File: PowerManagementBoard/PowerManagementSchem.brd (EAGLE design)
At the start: 160 x 100 mm, 95 parts, among them J1 D15S24A4GV00LF, U1 VX7805-500, U2 PYB20-Q24-S5, U3 PYB30-Q48-S5, U4 PYB30-Q48-S12, U5 3V3REG, U6 INA4180-SPLIT, U7 INA4180-SPLIT, U8 TEENSY-4.0SILK, U9 INA4180-SPLIT

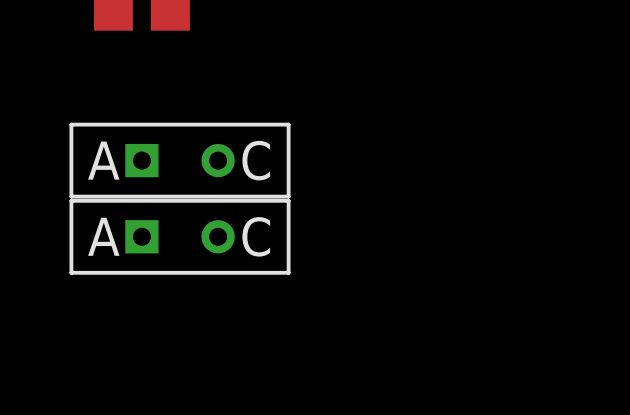
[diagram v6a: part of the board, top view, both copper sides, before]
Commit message: Added useless LED for test, names some nets.
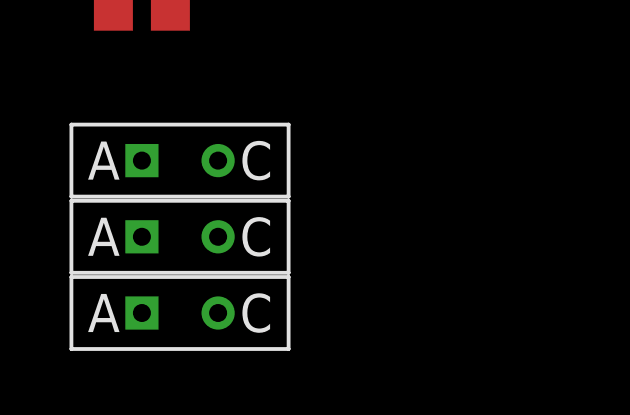
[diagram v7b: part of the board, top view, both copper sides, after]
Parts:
- added U$25: FLAT_LED, PowerManagementParts:FLAT_LED
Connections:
- removed net N$35: R20.1, U9.9
- removed net N$37: R21.1, U9.13
- removed net N$42: RN4.13, U$23.3
- net 12V: now also RN4.13, U$23.3
- net 12V-CAM: now also R20.1, U9.9
- net 12V-STA: now also R21.1, U9.13
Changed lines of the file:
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@@
 </element>
 <element name="U$21" library="PowerManagementParts" package="FLAT_LED" value="FLAT_LED" x="-261.62" y="-593.09"/>
+<element name="U$25" library="PowerManagementParts" package="FLAT_LED" value="FLAT_LED" x="-261.62" y="-595.63"/>
 </elements>
 <signals>
@@
 <contactref element="RN4" pad="14"/>
 <contactref element="U$22" pad="3"/>
+<contactref element="RN4" pad="13"/>
+<contactref element="U$23" pad="3"/>
+<wire x1="-225.425" y1="-529.7678" x2="-226.695" y2="-529.7678" width="0" layer="19" extent="1-1"/>
 <wire x1="-242.83" y1="-551.41" x2="-226.695" y2="-529.7678" width="0" layer="19" extent="1-1"/>
-<wire x1="-158.75" y1="-471.17" x2="-226.695" y2="-529.7678" width="0" layer="19" extent="1-1"/>
+<wire x1="-242.83" y1="-571.73" x2="-242.83" y2="-551.41" width="0" layer="19" extent="1-1"/>
+<wire x1="-158.75" y1="-471.17" x2="-225.425" y2="-529.7678" width="0" layer="19" extent="1-1"/>
 <wire x1="30.48" y1="74.93" x2="-158.75" y2="-471.17" width="0" layer="19" extent="1-1"/>
 <wire x1="-34.61" y1="149.86" x2="30.48" y2="74.93" width="0" layer="19" extent="1-1"/>
@@
 <signal name="12V-CAM">
 <contactref element="U$11" pad="PIN1"/>
+<contactref element="R20" pad="1"/>
+<contactref element="U9" pad="9"/>
+<wire x1="-242.722" y1="-556.26" x2="-227.33" y2="-509.0922" width="0" layer="19" extent="1-1"/>
+<wire x1="-147.828" y1="-422.91" x2="-227.33" y2="-509.0922" width="0" layer="19" extent="1-1"/>
 </signal>
 <signal name="12V-STA">
 <contactref element="U$12" pad="PIN1"/>
+<contactref element="R21" pad="1"/>
+<contactref element="U9" pad="13"/>
+<wire x1="-242.722" y1="-576.58" x2="-229.87" y2="-509.0922" width="0" layer="19" extent="1-1"/>
+<wire x1="-147.828" y1="-440.69" x2="-229.87" y2="-509.0922" width="0" layer="19" extent="1-1"/>
 </signal>
 <signal name="5V-DIG-STA">
@@
 <wire x1="-239.878" y1="-556.26" x2="-245.11" y2="-544.512" width="0" layer="19" extent="1-1"/>
 </signal>
-<signal name="N$35">
-<contactref element="R20" pad="1"/>
-<contactref element="U9" pad="9"/>
-<wire x1="-242.722" y1="-556.26" x2="-227.33" y2="-509.0922" width="0" layer="19" extent="1-1"/>
-</signal>
 <signal name="N$36">
 <contactref element="U$23" pad="4"/>
@@
 <wire x1="-239.878" y1="-576.58" x2="-245.11" y2="-564.832" width="0" layer="19" extent="1-1"/>
 </signal>
-<signal name="N$37">
-<contactref element="R21" pad="1"/>
-<contactref element="U9" pad="13"/>
-<wire x1="-242.722" y1="-576.58" x2="-229.87" y2="-509.0922" width="0" layer="19" extent="1-1"/>
-</signal>
 <signal name="5V-ACT-MAG">
 <contactref element="U$24" pad="PIN2"/>
@@
 <wire x1="-247.39" y1="-551.41" x2="-226.695" y2="-539.5722" width="0" layer="19" extent="1-1"/>
 </signal>
-<signal name="N$42">
-<contactref element="RN4" pad="13"/>
-<contactref element="U$23" pad="3"/>
-<wire x1="-242.83" y1="-571.73" x2="-225.425" y2="-529.7678" width="0" layer="19" extent="1-1"/>
-</signal>
 <signal name="N$43">

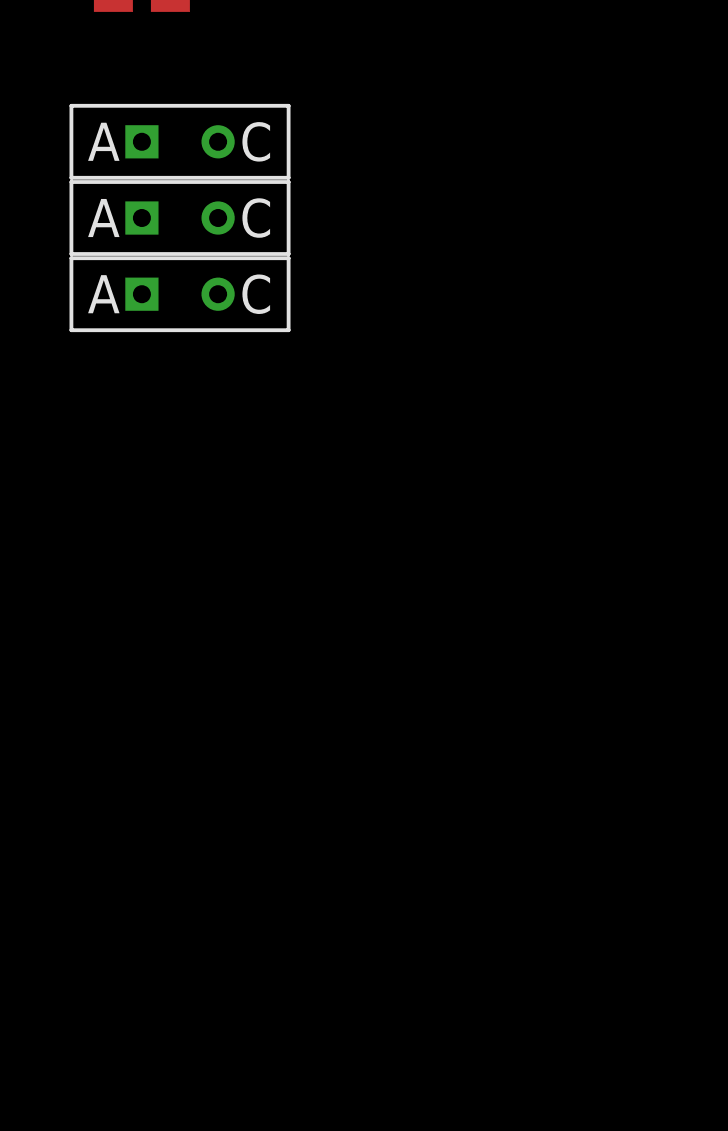
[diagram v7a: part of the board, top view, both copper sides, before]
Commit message: Finalized schematic. Ready for board layout
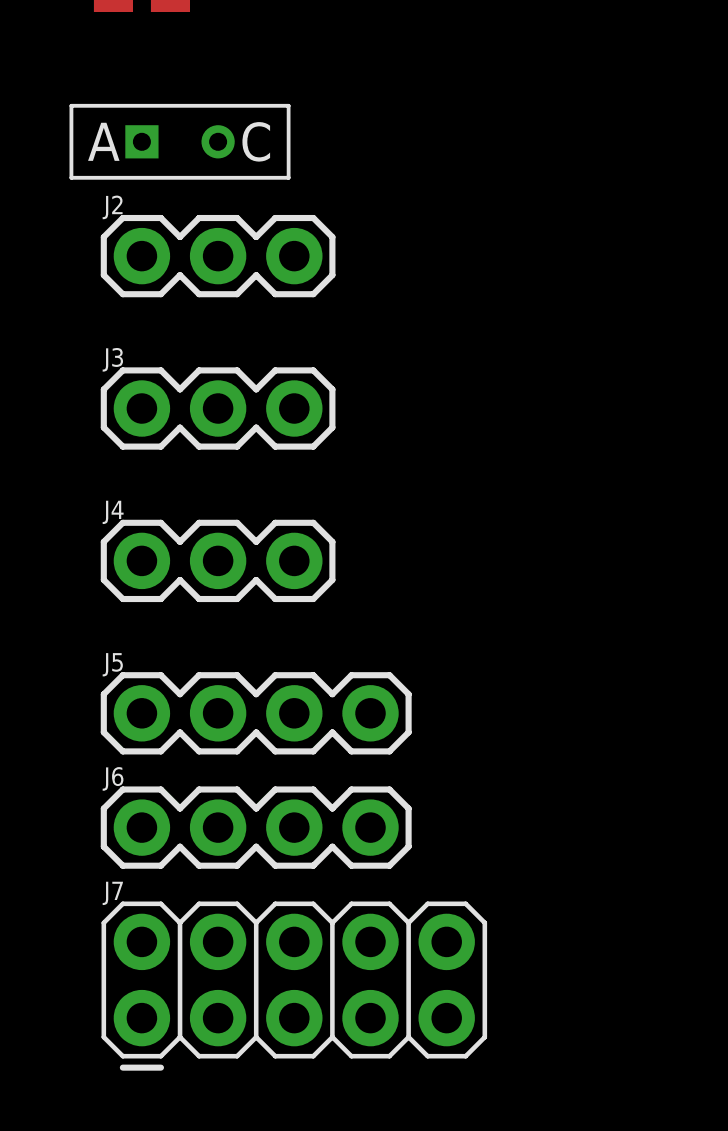
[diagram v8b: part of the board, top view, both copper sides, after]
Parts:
- removed U$21, U$25: FLAT_LED, PowerManagementParts:FLAT_LED
- added J2: 455-1750-1-ND, SparkFun-Connectors:1X03
- added J3, J4: (no value), SparkFun-Connectors:1X03
- added J5, J6: (no value), SparkFun-Connectors:1X04
- added J7: (no value), SparkFun-Connectors:2X5
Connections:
- removed net N$33: RN3.3
- net 12V: now also J7.10
- net 12V-CAM: now also J5.1
- net 12V-CAM-EN: now also RN3.3
- net 12V-STA: now also J6.1
- net 12V-STA-EN: now also RN3.4
- net 12V-STA-SNS: now also U9.14
- net 5V-ACT: now also J7.8
- net 5V-ACT-CAM: now also J5.3
- net 5V-ACT-LASER: now also J4.2
- net 5V-ACT-MAG: now also J2.2
- net 5V-ACT-STA: now also J6.3
- net 5V-ACT-TX: now also J3.2
- net 5V-DIG: now also J7.6
- net 5V-DIG-CAM: now also J5.4
- net 5V-DIG-LASER: now also J4.3
- net 5V-DIG-MAG: now also J2.3
- net 5V-DIG-STA: now also J6.4
- net 5V-DIG-TX: now also J3.3
- net GND: now also J2.1, J3.1, J4.1, J5.2, J6.2, J7.1
- net MNGR-3.3V: now also J7.4, U$20.ANODE
- net MNGR-5V: now also J7.2; no longer U$20.ANODE
- net SUPPLY_FOR_12V: now also J7.7
- net SUPPLY_FOR_5V-ACT: now also J7.5
- net SUPPLY_FOR_5V-DIG: now also J7.3
- net SUPPLY_FOR_MNGR: now also J7.9
